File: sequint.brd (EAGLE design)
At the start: 70 x 80 mm, 62 parts, among them IC1 STM32F10XCXT6, Q1 MOSFET-NCHANNELSMD, Q2 MOSFET-NCHANNELSMD, Q3 MOSFET-NCHANNELSMD, Q4 MOSFET-NCHANNELSMD, Q5 16MHz, U1 LSM330DLCTRLGA, U2 MCP73831, U4 NRF24L01SMD

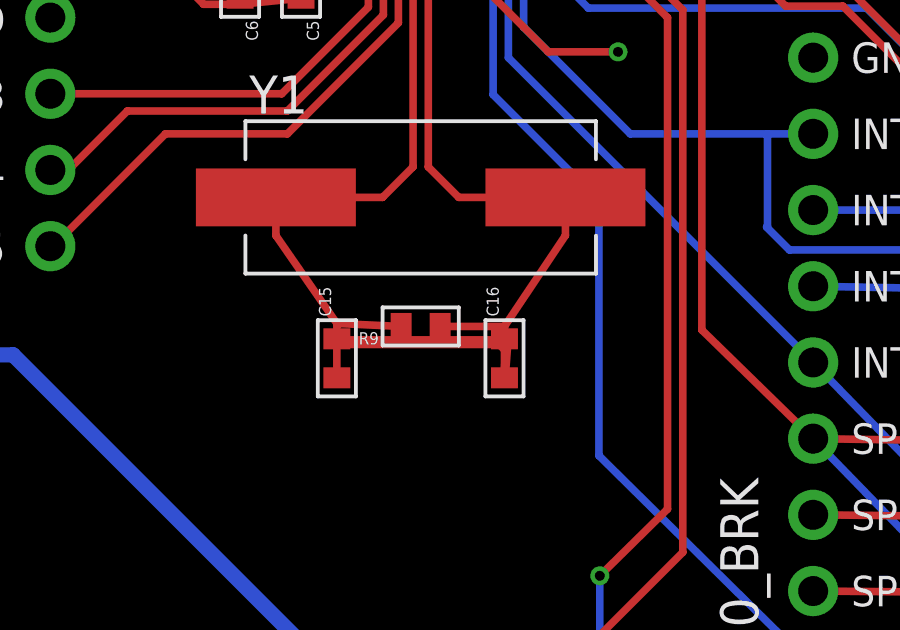
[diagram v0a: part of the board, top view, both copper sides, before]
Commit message: fixed DRC errors
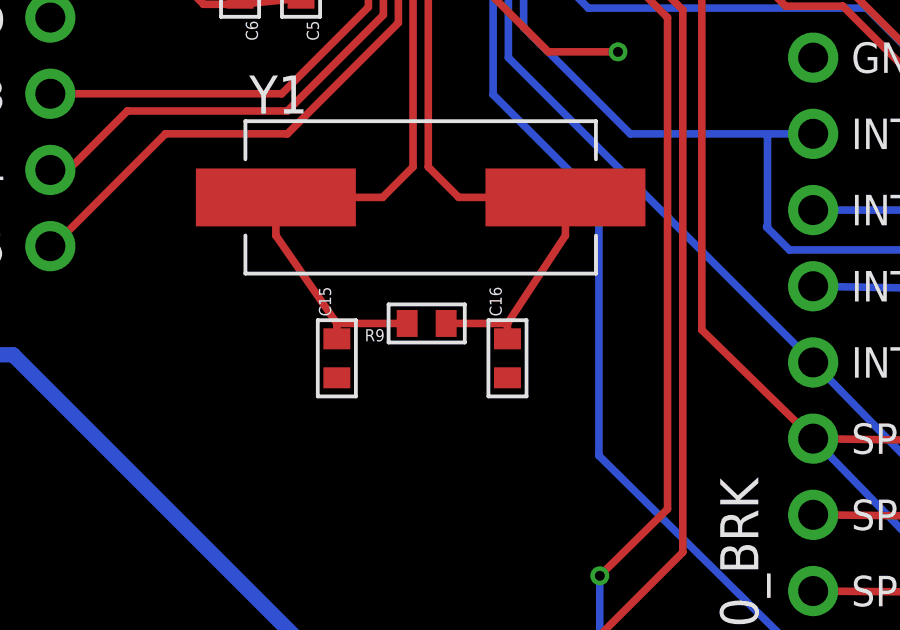
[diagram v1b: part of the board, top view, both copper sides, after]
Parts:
- moved R9 0.22 mm to (24.5, 30.8)
- moved C16 0.10 mm to (27.1, 29.6)
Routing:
- net GND: track 135.9 -> 126.9 mm
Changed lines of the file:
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@@
 <element name="Y1" library="nonolith" package="HC49UP" value="" x="24.2544" y="34.9656"/>
 <element name="C15" library="nonolith" package="0402" value="16pF" x="21.4604" y="29.6016" rot="R90"/>
-<element name="C16" library="nonolith" package="0402" value="16pF" x="27.0484" y="29.6016" rot="R90"/>
-<element name="R9" library="nonolith" package="0402" value="1MO" x="24.2544" y="30.6636" rot="R180"/>
+<element name="C16" library="nonolith" package="0402" value="16pF" x="27.1484" y="29.6016" rot="R90"/>
+<element name="R9" library="nonolith" package="0402" value="1MO" x="24.4544" y="30.7636" rot="R180"/>
 <element name="C17" library="nonolith" package="0402" value=".01uF" x="48.9178" y="50.9422" rot="R180"/>
 <element name="C18" library="nonolith" package="0402" value=".1uF" x="57.0458" y="60.3402"/>
@@
 <wire x1="52.4898" y1="57.4422" x2="51.5698" y2="58.5622" width="0.254" layer="1"/>
 <wire x1="51.1158" y1="60.5942" x2="51.5698" y2="60.8482" width="0.254" layer="1"/>
-<wire x1="21.4604" y1="28.9516" x2="21.4604" y2="30.1396" width="0.254" layer="1"/>
-<wire x1="26.7944" y1="30.1396" x2="27.0484" y2="29.8856" width="0.254" layer="1"/>
 <wire x1="4.29" y1="51.12" x2="4.29" y2="48.58" width="0.4064" layer="1"/>
 <wire x1="4.29" y1="48.58" x2="4.29" y2="46.04" width="0.4064" layer="1"/>
-<wire x1="27.0484" y1="29.8856" x2="27.0484" y2="28.9516" width="0.254" layer="1"/>
-<wire x1="26.7944" y1="30.1396" x2="21.4604" y2="30.1396" width="0.4064" layer="1"/>
 <wire x1="14.7804" y1="62.0156" x2="14.7804" y2="62.0676" width="0.254" layer="1"/>
 <wire x1="14.7804" y1="62.0676" x2="14.8564" y2="62.1436" width="0.254" layer="1"/>
@@
 <wire x1="53.835" y1="34.102" x2="54.328" y2="34.229" width="0.3048" layer="1"/>
 <wire x1="54.328" y1="32.197" x2="54.328" y2="31.435" width="0.3048" layer="1"/>
-<wire x1="27.1364" y1="30.1396" x2="27.0484" y2="28.9516" width="0.3048" layer="1"/>
 <wire x1="57.996" y1="37.023" x2="57.63" y2="37.023" width="0.254" layer="1"/>
 <wire x1="57.63" y1="37.023" x2="57.63" y2="34.737" width="0.3048" layer="1"/>
@@
 <wire x1="24.5084" y1="35.9816" x2="25.5244" y2="34.9656" width="0.254" layer="1"/>
 <wire x1="25.5244" y1="34.9656" x2="29.0804" y2="34.9656" width="0.254" layer="1"/>
-<wire x1="24.9044" y1="30.6636" x2="27.0484" y2="30.6636" width="0.254" layer="1"/>
-<wire x1="27.0484" y1="30.6636" x2="29.0804" y2="33.6956" width="0.254" layer="1"/>
+<wire x1="25.1044" y1="30.7636" x2="27.1484" y2="30.7636" width="0.254" layer="1"/>
+<wire x1="27.1484" y1="30.7636" x2="29.0804" y2="33.6956" width="0.254" layer="1"/>
 <wire x1="29.0804" y1="33.6956" x2="29.0804" y2="34.9656" width="0.254" layer="1"/>
-<wire x1="27.0484" y1="30.2516" x2="27.0484" y2="30.6636" width="0.254" layer="1"/>
+<wire x1="27.1484" y1="30.2516" x2="27.1484" y2="30.7636" width="0.254" layer="1"/>
 </signal>
 <signal name="PD0">
@@
 <wire x1="24.0004" y1="35.9816" x2="24.0004" y2="43.6616" width="0.254" layer="1"/>
 <wire x1="24.0004" y1="43.6616" x2="24.0124" y2="43.6736" width="0.254" layer="1"/>
-<wire x1="23.6044" y1="30.6636" x2="21.4604" y2="30.7636" width="0.254" layer="1"/>
+<wire x1="23.8044" y1="30.7636" x2="21.4604" y2="30.7636" width="0.254" layer="1"/>
 <wire x1="21.4604" y1="30.7636" x2="19.4284" y2="33.6956" width="0.254" layer="1"/>
 <wire x1="19.4284" y1="33.6956" x2="19.4284" y2="34.9656" width="0.254" layer="1"/>

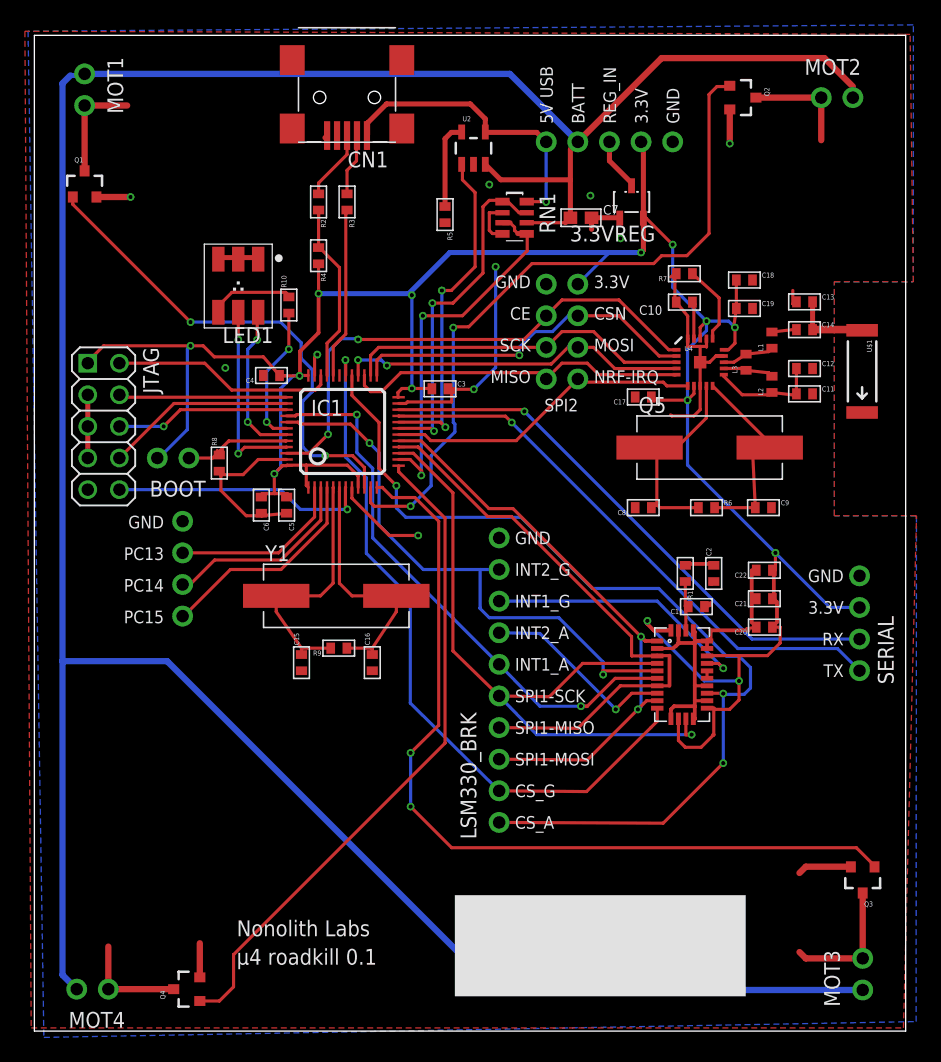
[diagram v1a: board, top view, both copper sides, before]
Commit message: added snubber diodes in SOD523 aka tiny
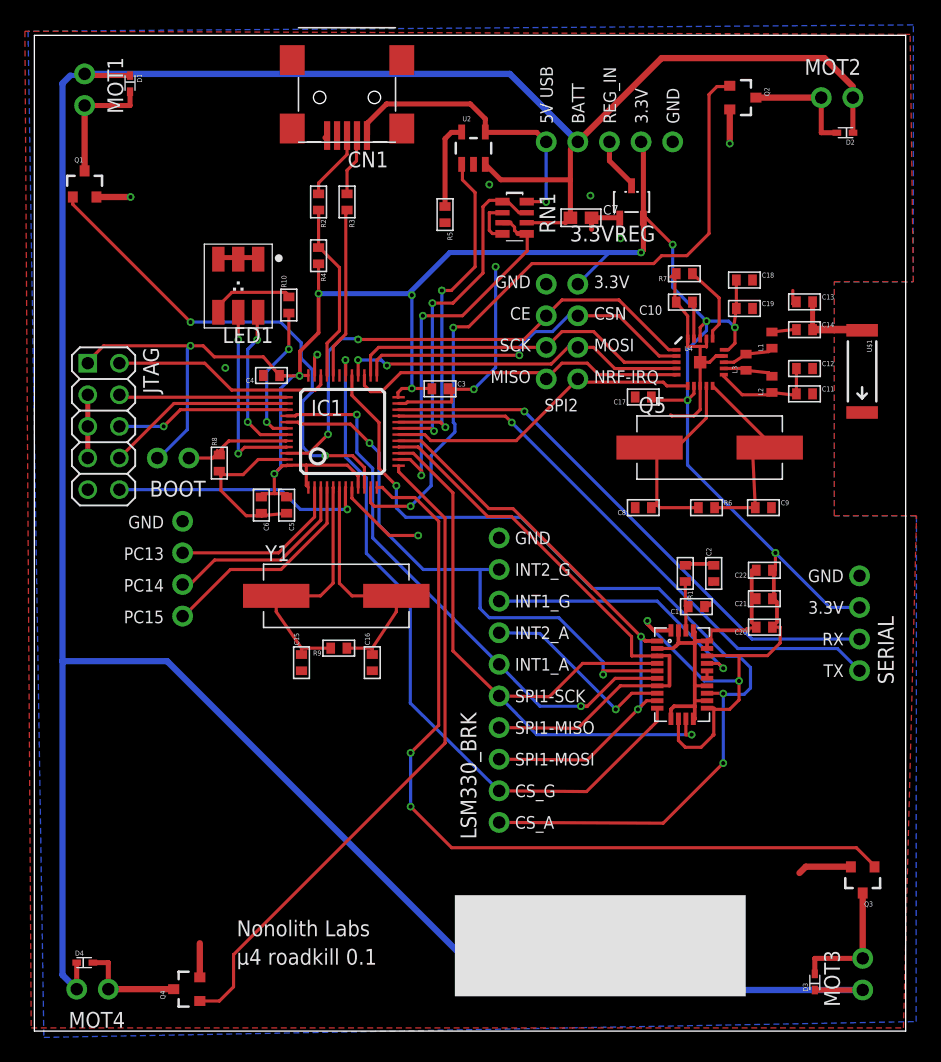
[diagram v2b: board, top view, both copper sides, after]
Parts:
- added D1, D2, D3, D4: (no value), SparkFun-DiscreteSemi:SOD523
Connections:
- net VBATT: now also D1.C, D2.C, D3.C, D4.C
- net VL-1: now also D1.A
- net VL-2: now also D2.A
- net VL-3: now also D3.A
- net VL-4: now also D4.A
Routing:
- net VBATT: track 237.3 -> 249.9 mm
- net VL-1: track 8.67 -> 10.0 mm
- net VL-2: track 8.67 -> 9.32 mm
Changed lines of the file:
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@@
 <element name="JP1" library="nonolith" package="1X04_ROUND" value="PORTC" x="11.91" y="37.15" smashed="yes" rot="R90"/>
 <element name="U$1" library="SparkFun-RF" package="ANTENNA-CHIP5" value="ANTENNA2SMD5" x="66.5" y="53" rot="R270"/>
+<element name="D1" library="SparkFun-DiscreteSemi" package="SOD523" value="" x="7.685" y="76.17" rot="R270"/>
+<element name="D2" library="SparkFun-DiscreteSemi" package="SOD523" value="" x="65.17" y="72.175" rot="R180"/>
+<element name="D3" library="SparkFun-DiscreteSemi" package="SOD523" value="" x="62.7" y="3.9" rot="R90"/>
+<element name="D4" library="SparkFun-DiscreteSemi" package="SOD523" value="" x="4" y="5.5"/>
 </elements>
 <signals>
@@
 <contactref element="MOT4" pad="1"/>
 <wire x1="11.191" y1="3.368" x2="5.941" y2="3.368" width="0.508" layer="1"/>
-<wire x1="5.941" y1="3.368" x2="5.941" y2="6.788" width="0.508" layer="1"/>
+<contactref element="D4" pad="A"/>
+<wire x1="4.7" y1="5.5" x2="5.941" y2="5.5" width="0.4064" layer="1"/>
+<wire x1="5.941" y1="5.5" x2="5.941" y2="3.368" width="0.4064" layer="1"/>
 </signal>
 <signal name="VL-3">
 <contactref element="Q3" pad="3"/>
 <contactref element="MOT3" pad="2"/>
-<wire x1="66.548" y1="5.842" x2="61.976" y2="5.842" width="0.508" layer="1"/>
-<wire x1="61.976" y1="5.842" x2="61.468" y2="6.35" width="0.508" layer="1"/>
 <wire x1="66.548" y1="11.092" x2="66.548" y2="5.842" width="0.508" layer="1"/>
+<contactref element="D3" pad="A"/>
+<wire x1="66.548" y1="5.842" x2="62.7" y2="5.842" width="0.4064" layer="1"/>
+<wire x1="62.7" y1="5.842" x2="62.7" y2="4.6" width="0.4064" layer="1"/>
 </signal>
 <signal name="VL-2">
 <contactref element="Q2" pad="3"/>
 <contactref element="MOT2" pad="1"/>
-<wire x1="63.218" y1="74.996" x2="63.218" y2="71.576" width="0.508" layer="1"/>
 <wire x1="63.218" y1="74.996" x2="57.968" y2="74.996" width="0.508" layer="1"/>
+<contactref element="D2" pad="A"/>
+<wire x1="64.47" y1="72.175" x2="63.218" y2="72.175" width="0.4064" layer="1"/>
+<wire x1="63.218" y1="72.175" x2="63.218" y2="74.996" width="0.4064" layer="1"/>
 </signal>
 <signal name="VL-1">
@@
 <contactref element="MOT1" pad="2"/>
 <wire x1="4.036" y1="74.361" x2="4.036" y2="69.111" width="0.508" layer="1"/>
-<wire x1="4.036" y1="74.361" x2="7.456" y2="74.361" width="0.508" layer="1"/>
+<contactref element="D1" pad="A"/>
+<wire x1="4.036" y1="74.361" x2="7.685" y2="74.361" width="0.4064" layer="1"/>
+<wire x1="7.685" y1="74.361" x2="7.685" y2="75.47" width="0.4064" layer="1"/>
 </signal>
 <signal name="VBATT">
@@
 <wire x1="10.668" y1="29.718" x2="37.084" y2="3.302" width="0.508" layer="16"/>
 <wire x1="37.084" y1="3.302" x2="66.548" y2="3.302" width="0.508" layer="16"/>
+<contactref element="D1" pad="C"/>
+<contactref element="D2" pad="C"/>
+<contactref element="D3" pad="C"/>
+<contactref element="D4" pad="C"/>
+<wire x1="7.685" y1="76.77" x2="4.036" y2="76.77" width="0.4064" layer="1"/>
+<wire x1="4.036" y1="76.77" x2="4.036" y2="76.901" width="0.4064" layer="1"/>
+<wire x1="3.4" y1="5.5" x2="3.401" y2="5.5" width="0.4064" layer="1"/>
+<wire x1="3.401" y1="5.5" x2="3.401" y2="3.368" width="0.4064" layer="1"/>
+<wire x1="62.7" y1="3.3" x2="66.548" y2="3.3" width="0.4064" layer="1"/>
+<wire x1="66.548" y1="3.3" x2="66.548" y2="3.302" width="0.4064" layer="1"/>
+<wire x1="65.77" y1="72.175" x2="65.758" y2="72.175" width="0.4064" layer="1"/>
+<wire x1="65.758" y1="72.175" x2="65.758" y2="74.996" width="0.4064" layer="1"/>
 </signal>
 <signal name="USB+">

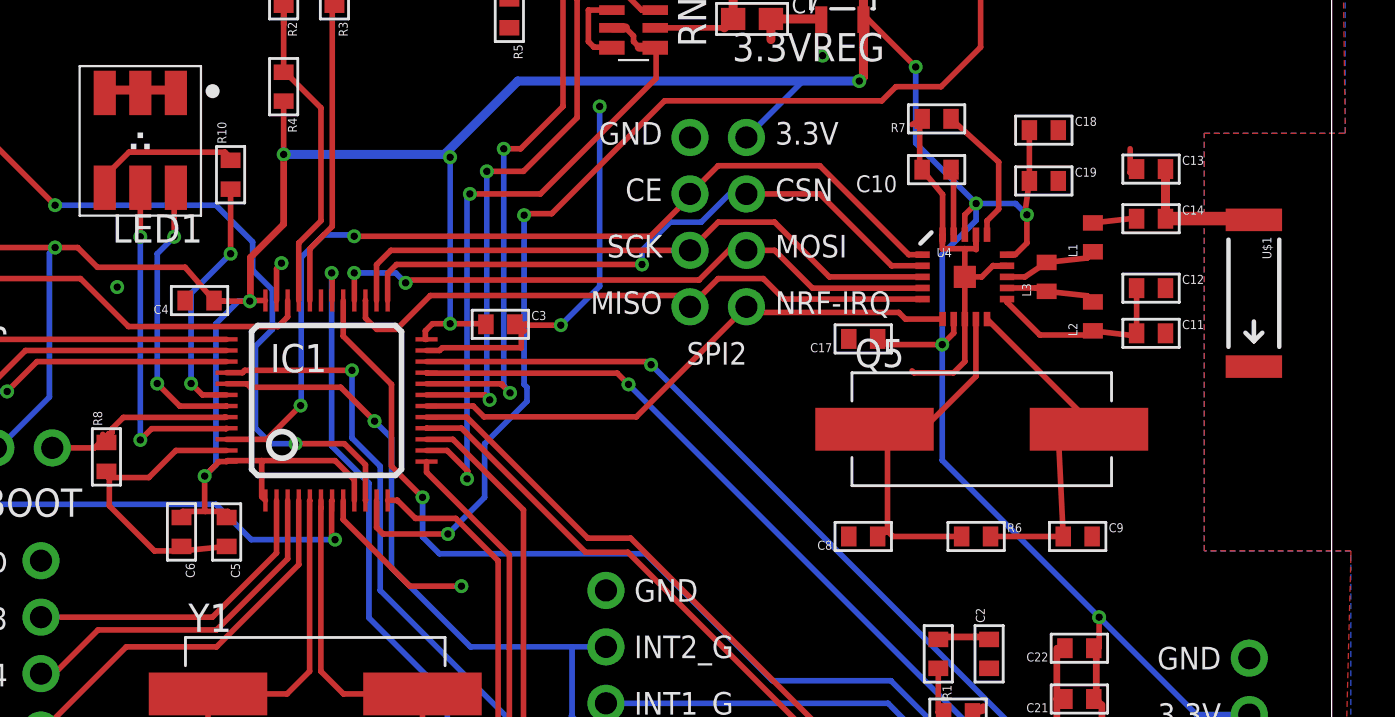
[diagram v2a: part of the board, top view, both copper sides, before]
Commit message: Pack radio tighter. Add GND vias
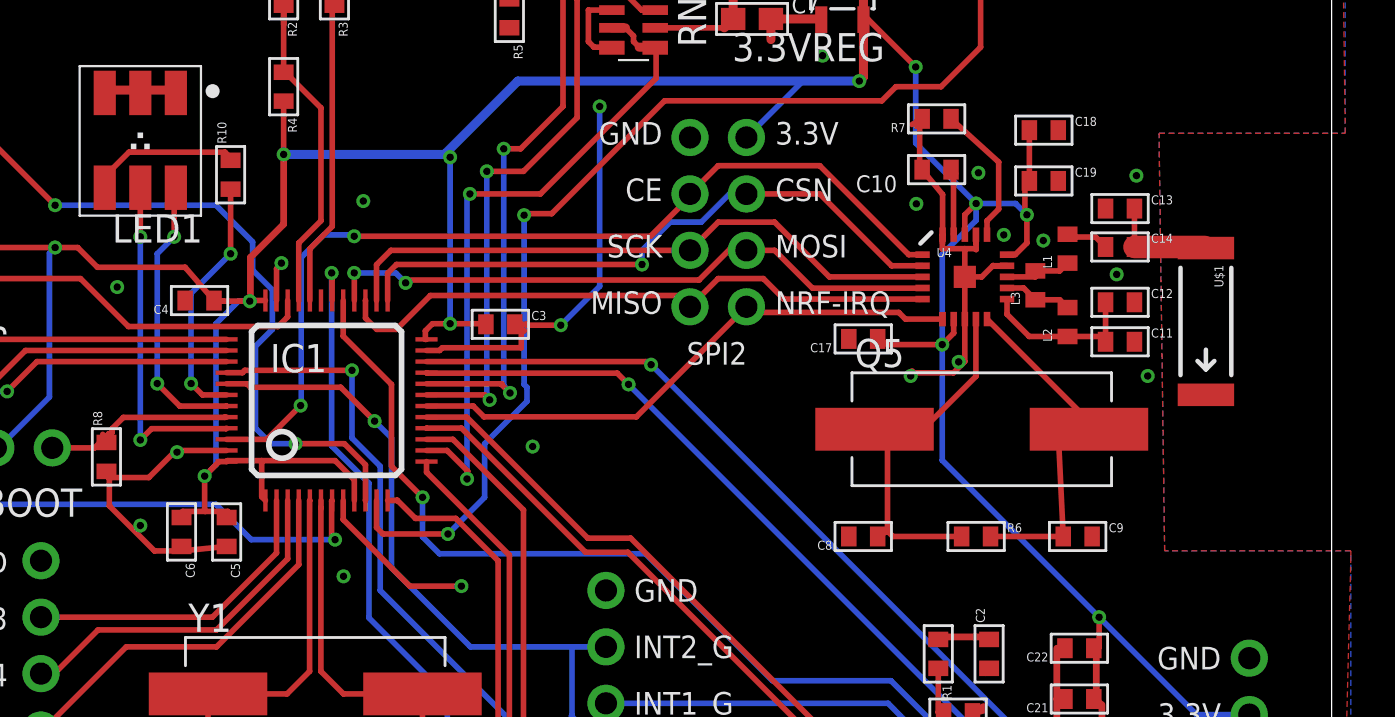
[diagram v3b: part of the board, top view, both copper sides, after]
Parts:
- moved U$1 2.50 mm to (64.3, 51.7)
- moved C13 2.26 mm to (60.5, 56.8)
- moved C14 1.89 mm to (60.5, 55.1)
- moved C12 1.53 mm to (60.5, 52.6)
- moved C11 1.45 mm to (60.5, 50.8)
- moved L1 1.25 mm to (58.1, 55.0)
- moved L2 1.17 mm to (58.1, 51.7)
- moved L3 0.63 mm to (56.7, 53.4)
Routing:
- net ANT: track 8.73 -> 4.96 mm
- net GND: track 126.9 -> 125.2 mm, vias 10 -> 24
- net VDD_PA: track 8.72 -> 7.41 mm
- net ANT2: track 4.20 -> 3.14 mm
- net ANT1: track 4.02 -> 3.09 mm
